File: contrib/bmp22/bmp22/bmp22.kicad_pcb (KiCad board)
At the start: 2 copper layers, 76 parts, among them J201 Conn_01x10_Male, J202 PH1x4, J301 USB_C_Receptacle_USB2.0, J302 Conn_ARM_JTAG_SWD_10, Q201 DMG1023UV-7, Q202 DMG1024UV-7, Q203 DMG1024UV-7, SW301 SW_DIP_x01, U101 LP2985-3.3, U201 SN74LVC2T45DCUR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

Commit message: created layout
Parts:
- removed Q202: DMG1024UV-7, Package_TO_SOT_SMD:SOT-563
- added FID1: Fiducial, Fiducial:Fiducial_1mm_Mask2mm, F.Cu at (121.5, 121.5)
- added FID2: Fiducial, Fiducial:Fiducial_1mm_Mask2mm, F.Cu at (168.5, 138.5)
- added FID3: Fiducial, Fiducial:Fiducial_1mm_Mask2mm, F.Cu at (168.5, 121.5)
- added FID4: Fiducial, Fiducial:Fiducial_1mm_Mask2mm, B.Cu at (121.5, 123.0)
- added FID5: Fiducial, Fiducial:Fiducial_1mm_Mask2mm, B.Cu at (160.5, 138.5)
- added FID6: Fiducial, Fiducial:Fiducial_1mm_Mask2mm, B.Cu at (121.5, 138.5)
- added H1: MountingHole, MountingHole:MountingHole_2.7mm_M2.5_DIN965, F.Cu at (124.5, 137.5)
- added H2: MountingHole, MountingHole:MountingHole_2.7mm_M2.5_DIN965, F.Cu at (124.5, 122.5)
- added H3: MountingHole, MountingHole:MountingHole_2.7mm_M2.5_DIN965, F.Cu at (164.0, 137.5)
- added H4: MountingHole, MountingHole:MountingHole_2.7mm_M2.5_DIN965, F.Cu at (164.0, 122.5)
- J202: moved to B.Cu
- TP301, TP302, TP303, TP304, TP305, TP306, TP307, TP309: footprint TestPoint:TestPoint_Pad_1.0x1.0mm -> TestPoint:TestPoint_Pad_D1.5mm; moved to B.Cu
- TP308: value DIO -> SWDIO; footprint TestPoint:TestPoint_Pad_1.0x1.0mm -> TestPoint:TestPoint_Pad_D1.5mm; moved to B.Cu
- moved C204 53.9 mm to (157.9, 133.3)
- moved R209 52.2 mm to (161.0, 134.1), turned to 180 degrees
- moved R308 49.3 mm to (134.4, 133.1)
- moved Q203 49.1 mm to (151.4, 124.8)
- moved TP308 48.7 mm to (134.5, 134.5), turned to 180 degrees
- moved R205 48.2 mm to (156.7, 138.0), turned to 180 degrees
- moved C208 47.7 mm to (157.9, 129.3)
- moved R206 46.9 mm to (160.5, 128.8), turned to 180 degrees
- moved R211 46.4 mm to (153.5, 124.8), turned to 270 degrees
- moved R303 45.6 mm to (133.3, 130.0), turned to 180 degrees
- moved C307 44.8 mm to (139.7, 137.2), turned to 270 degrees
- moved TP301 44.4 mm to (137.0, 134.5), turned to 90 degrees
- moved C203 43.8 mm to (155.4, 133.3), turned to 180 degrees
- moved JP201 43.1 mm to (156.7, 137.0), turned to 180 degrees
- moved C205 42.9 mm to (155.4, 125.2), turned to 180 degrees
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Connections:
- net /Sheet5F25207C/USB+ renamed /Sheet5F25207C/USB_P
- net /Sheet5F25207C/USB- renamed /Sheet5F25207C/USB_N
- D301 pad 1: Net-(D301-Pad1) -> GND
- D301 pad 2: +3V3 -> Net-(D301-Pad2)
- D302 pad 1: Net-(D302-Pad1) -> GND
- D302 pad 2: /Sheet5F25207C/LED0 -> Net-(D302-Pad2)
- D303 pad 1: Net-(D303-Pad1) -> GND
- D303 pad 2: /Sheet5F25207C/LED1 -> Net-(D303-Pad2)
- D304 pad 1: Net-(D304-Pad1) -> GND
- D304 pad 2: /Sheet5F25207C/LED2 -> Net-(D304-Pad2)
- Q201 pad 3: (no net) -> TPWR
- Q201 pad 4: (no net) -> Net-(Q201-Pad1)
- Q201 pad 5: (no net) -> PWR_BR
- R208 pad 2: xRXD -> xTXD
- R209 pad 2: xTXD -> xRXD
- R311 pad 1: Net-(D301-Pad1) -> +3V3
- R311 pad 2: GND -> Net-(D301-Pad2)
- R312 pad 1: Net-(D302-Pad1) -> /Sheet5F25207C/LED0
- R312 pad 2: GND -> Net-(D302-Pad2)
- R313 pad 1: Net-(D303-Pad1) -> /Sheet5F25207C/LED1
- R313 pad 2: GND -> Net-(D303-Pad2)
- R314 pad 1: Net-(D304-Pad1) -> /Sheet5F25207C/LED2
- R314 pad 2: GND -> Net-(D304-Pad2)
- U301 pad 1: /Sheet5F25207C/USBx2- -> /Sheet5F25207C/USBx2+
- U301 pad 3: /Sheet5F25207C/USBx2+ -> /Sheet5F25207C/USBx2-
- U301 pad 4: /Sheet5F25207C/USBx1+ -> /Sheet5F25207C/USBx1-
- U301 pad 6: /Sheet5F25207C/USBx1- -> /Sheet5F25207C/USBx1+
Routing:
- net +3V3: track 0.00 -> 109.0 mm, vias 0 -> 10
- net iTXD: track 0.00 -> 41.3 mm, vias 0 -> 4
- net /Sheet5F25207C/~RST: track 0.00 -> 35.3 mm, vias 0 -> 1
- net TPWR: track 0.00 -> 31.9 mm, vias 0 -> 3
- net +5V: track 0.00 -> 28.6 mm, vias 0 -> 4
- net iRXD: track 0.00 -> 24.8 mm, vias 0 -> 4
- net xTPWR: track 0.00 -> 22.8 mm, vias 0 -> 2
- net /Sheet5F25207C/TRACESWO: track 0.00 -> 20.8 mm, vias 0 -> 2
- net KEY: track 0.00 -> 20.2 mm, vias 0 -> 2
- net iTDO: track 0.00 -> 18.6 mm, vias 0 -> 2
- net /Sheet5F25207C/SWDCLK: track 0.00 -> 17.3 mm, vias 0 -> 2
- net /Sheet5F25207C/VBUS: track 0.00 -> 15.0 mm, vias 0 -> 2
- net iTMS_DIR: track 0.00 -> 14.7 mm, vias 0 -> 2
- net Net-(R309-Pad2): track 0.00 -> 13.6 mm, vias 0 -> 2
- net iTMS: track 0.00 -> 12.8 mm, vias 0 -> 2
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- added copper zone on B.Cu, net GND
- added copper zone on F.Cu, net GND
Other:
- board outline added: 50 x 20 mm
- net class Default: clearance 0.2 -> 0.15; trace_width 0.25 -> 0.2; via_dia 0.8 -> 0.6; via_drill 0.4 -> 0.3
- rule trace_clearance: 0.2 -> 0.15
- rule trace_min: 0.2 -> 0.15
- board text added: "GND"
- board text added: "RXD"
- board text added: "TPWR"
- board text added: "TXD"

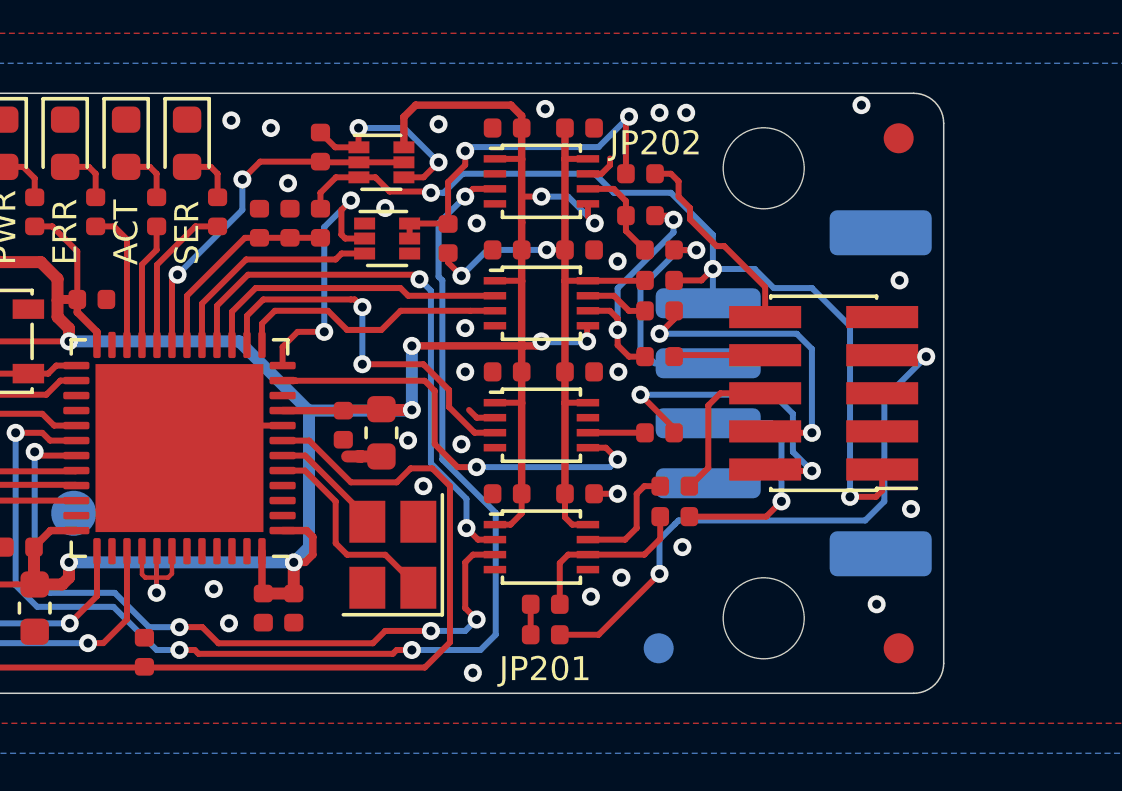
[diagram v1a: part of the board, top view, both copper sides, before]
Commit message: changed silkscreen
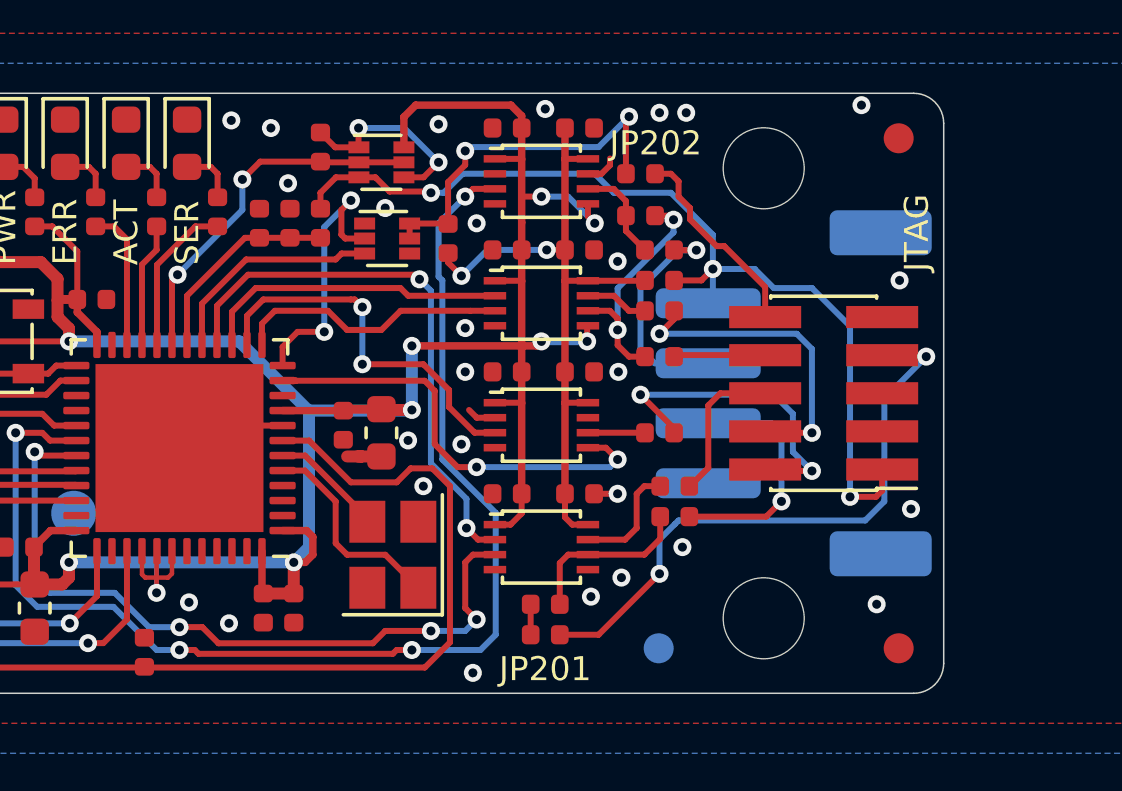
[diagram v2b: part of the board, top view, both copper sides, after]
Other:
- board text added: "BlackMagic Probe V.2.2"
- board text added: "JTAG"
- board text added: "by Rico & David"
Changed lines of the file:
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@@
   (general
     (thickness 1.6)
-    (drawings 14)
+    (drawings 17)
     (tracks 670)
     (zones 0)
@@
     (34 B.Paste user hide)
     (35 F.Paste user hide)
-    (36 B.SilkS user hide)
+    (36 B.SilkS user)
     (37 F.SilkS user)
     (38 B.Mask user hide)
@@
     (pad_to_mask_clearance 0.05)
     (aux_axis_origin 0 0)
-    (visible_elements 7FFFFFFF)
+    (visible_elements 7FFBFFFF)
     (pcbplotparams
       (layerselection 0x010fc_ffffffff)
@@
       (effects (font (size 1 1) (thickness 0.15)) (justify mirror))
     )
-    (fp_text value USBx1+ (at 0 1.079 180) (layer B.SilkS)
+    (fp_text value USBx1+ (at -0.072 1.317 180) (layer B.SilkS)
       (effects (font (size 0.8 0.8) (thickness 0.15)) (justify right mirror))
     )
@@
       (effects (font (size 1 1) (thickness 0.15)) (justify mirror))
     )
-    (fp_text value USBx1- (at 0 1.206 180) (layer B.SilkS)
+    (fp_text value USBx1- (at -0.413 1.317) (layer B.SilkS)
       (effects (font (size 0.8 0.8) (thickness 0.15)) (justify right mirror))
     )
+    (fp_circle (center 0 0) (end 0 -0.95) (layer B.SilkS) (width 0.12))
+    (fp_circle (center 0 0) (end 1.25 0) (layer B.CrtYd) (width 0.05))
     (fp_text user %R (at 0 1.65 90) (layer B.Fab)
       (effects (font (size 1 1) (thickness 0.15)) (justify mirror))
     )
-    (fp_circle (center 0 0) (end 1.25 0) (layer B.CrtYd) (width 0.05))
-    (fp_circle (center 0 0) (end 0 -0.95) (layer B.SilkS) (width 0.12))
     (pad 1 smd circle (at 0 0 90) (size 1.5 1.5) (layers B.Cu B.Mask)
       (net 25 /Sheet5F25207C/USBx1-))
@@
     )
   )
+  (gr_text "by Rico & David" (at 136.525 139.192) (layer B.SilkS)
+    (effects (font (size 0.8 0.8) (thickness 0.15)) (justify mirror))
+  )
+  (gr_text "BlackMagic\nProbe V.2.2" (at 138.1125 122.7455) (layer B.SilkS)
+    (effects (font (size 0.8 0.8) (thickness 0.15)) (justify mirror))
+  )
+  (gr_text JTAG (at 169.1005 124.6505 90) (layer F.SilkS)
+    (effects (font (size 0.8 0.8) (thickness 0.15)))
+  )
   (gr_text GND (at 158.75 132.969) (layer B.SilkS)
     (effects (font (size 0.8 0.8) (thickness 0.15)) (justify left mirror))
@@
   (via (at 131.445 128.143) (size 0.6) (drill 0.3) (layers F.Cu B.Cu) (net 1))
   (via (at 138.176 137.033) (size 0.6) (drill 0.3) (layers F.Cu B.Cu) (net 1))
-  (via (at 145.669 136.525) (size 0.6) (drill 0.3) (layers F.Cu B.Cu) (net 1))
+  (via (at 144.8435 136.9695) (size 0.6) (drill 0.3) (layers F.Cu B.Cu) (net 1))
   (segment (start 145.276 131.076) (end 144.526 131.826) (width 0.2) (layer F.Cu) (net 1))
   (segment (start 147.9635 131.076) (end 145.276 131.076) (width 0.2) (layer F.Cu) (net 1))

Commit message: layouted new changes, added keepout for tag connect, improved gnd plane
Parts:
- added R315: DNP, Resistor_SMD:R_0402_1005Metric, F.Cu at (145.8, 138.8)
- added R316: DNP, Resistor_SMD:R_0402_1005Metric, F.Cu at (145.8, 137.7)
- added R317: 0, Resistor_SMD:R_0402_1005Metric, F.Cu at (145.8, 136.6)
- added R318: 330, Resistor_SMD:R_0402_1005Metric, F.Cu at (140.7, 124.5)
- added R319: 0, Resistor_SMD:R_0402_1005Metric, F.Cu at (145.3, 124.5)
- R314: value 330 -> DNP
- moved R311 4.47 mm to (135.9, 121.6)
- moved R313 2.74 mm to (142.2, 121.7)
- moved R312 2.11 mm to (145.3, 121.9)
- moved C103 2.10 mm to (135.9, 124.4)
- moved D302 1.92 mm to (146.7, 121.7)
- moved D301 0.98 mm to (137.7, 121.7)
- moved C301 0.96 mm to (142.4, 138.6)
- moved D303 0.95 mm to (143.7, 121.7)
- moved R314 0.57 mm to (141.9, 124.5)
- moved R204 0.44 mm to (160.6, 133.1)
- moved R209 0.19 mm to (161.0, 134.3)
- moved C307 0.10 mm to (139.6, 137.2)
- turned C203 to 0 degrees
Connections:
- net /Sheet5F25207C/LED2 renamed /Sheet5F25207C/LED2_OLD
- U302 pad 27: Net-(U302-Pad27) -> /Sheet5F25207C/LED2_NEW
- U302 pad 41: +3V3 -> /Sheet5F25207C/B0
- U302 pad 42: +3V3 -> /Sheet5F25207C/B1
- U302 pad 43: Net-(U302-Pad43) -> /Sheet5F25207C/B2
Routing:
- net GND: track 7.85 -> 22.0 mm, vias 48 -> 58
- net /Sheet5F25207C/LED2_NEW: track 0.00 -> 8.58 mm, vias 0 -> 2
- net /Sheet5F25207C/B0: track 0.00 -> 4.17 mm
- net iTDO: track 18.6 -> 22.5 mm, vias 2 -> 4
- net TPWR: track 31.9 -> 28.9 mm
- net /Sheet5F25207C/B1: track 0.00 -> 2.87 mm
- net /Sheet5F25207C/LED2_OLD: track 4.74 -> 7.57 mm, vias 0 -> 2
- net /Sheet5F25207C/LED1: track 4.15 -> 6.79 mm
- net iTXD: track 41.3 -> 43.4 mm
- net KEY: track 20.2 -> 18.3 mm
- net /Sheet5F25207C/B2: track 0.00 -> 1.55 mm
- net /Sheet5F25207C/LED0: track 5.22 -> 6.63 mm
- net /Sheet5F25207C/SWDCLK: track 17.3 -> 16.2 mm
- net Net-(D304-Pad2): track 1.90 -> 2.73 mm
- net /Sheet5F25207C/TRACESWO: track 20.8 -> 21.5 mm
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
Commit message: updated schematic and layout
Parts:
- removed R315, R316: DNP, Resistor_SMD:R_0402_1005Metric
- removed R317, R319: 0, Resistor_SMD:R_0402_1005Metric
- removed R318: 330, Resistor_SMD:R_0402_1005Metric
- R314: value DNP -> 330
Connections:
- net /Sheet5F25207C/LED2_OLD renamed /Sheet5F25207C/LED2
- U302 pad 27: /Sheet5F25207C/LED2_NEW -> Net-(U302-Pad27)
- U302 pad 41: /Sheet5F25207C/B0 -> +3V3
- U302 pad 42: /Sheet5F25207C/B1 -> +3V3
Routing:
- net GND: track 22.0 -> 31.2 mm, vias 58 -> 59
- net /Sheet5F25207C/LED2_NEW: track 8.58 -> 0.00 mm, vias 2 -> 0
- net /Sheet5F25207C/B0: track 4.17 -> 0.00 mm
- net /Sheet5F25207C/LED2: track 7.57 -> 3.77 mm, vias 2 -> 0
- net /Sheet5F25207C/B1: track 2.87 -> 0.00 mm
- net iTDO: track 22.5 -> 19.9 mm, vias 4 -> 2
- net /Sheet5F25207C/B2: track 1.55 -> 0.00 mm
- net PWR_BR: track 11.8 -> 12.8 mm, vias 2 -> 0
- net Net-(C309-Pad1): track 6.87 -> 7.66 mm
